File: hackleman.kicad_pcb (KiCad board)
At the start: 2 copper layers, 99.5 x 50 mm, 188 parts, among them SW1 SW_DIP_x05

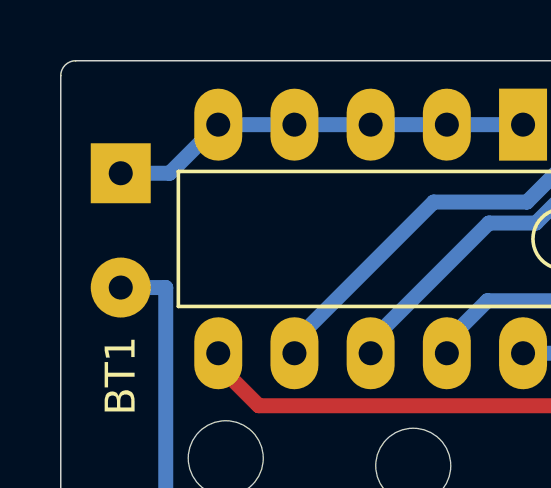
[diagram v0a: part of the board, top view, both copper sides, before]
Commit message: added plus and minus for battery
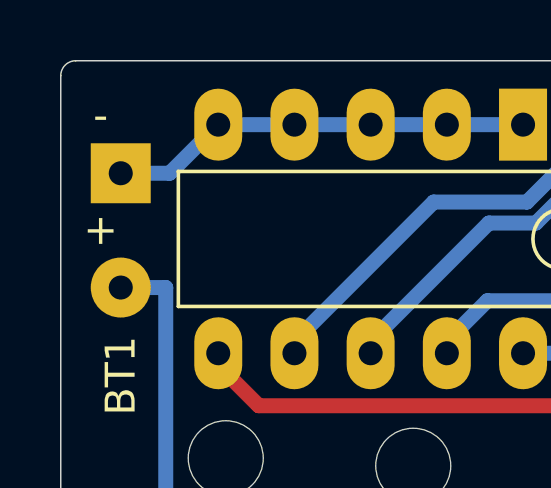
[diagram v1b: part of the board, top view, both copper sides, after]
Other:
- board text added: "+"
- board text added: "-"
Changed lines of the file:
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@@
-(kicad_pcb (version 20171130) (host pcbnew "(5.1.0)-1")
+(kicad_pcb (version 20171130) (host pcbnew 5.1.4-e60b266~84~ubuntu18.04.1)
   (general
     (thickness 1.6)
-    (drawings 2510)
+    (drawings 2512)
     (tracks 275)
     (zones 0)
@@
   )
   (setup
-    (last_trace_width 0.5)
+    (last_trace_width 0.25)
     (user_trace_width 0.5)
     (trace_clearance 0.2)
@@
       (net 2 "Net-(BT1-Pad1)"))
   )
+  (gr_text + (at 36.83 40.64) (layer F.SilkS)
+    (effects (font (size 1 1) (thickness 0.15)))
+  )
+  (gr_text - (at 36.83 36.83) (layer F.SilkS)
+    (effects (font (size 1 1) (thickness 0.15)))
+  )
   (gr_text 5 (at 125.152271 67.473478) (layer B.SilkS)
